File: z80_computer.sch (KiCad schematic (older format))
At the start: 14 parts, among them SW0 SW_Push, U0 Z80CPU, U1 CY62256NLL-55SNXI, U2 AT28C256_40PIN_ZIF, U4 SN74LS04N, U5 SN74LS00N, Y0 Crystal 6 MHZ

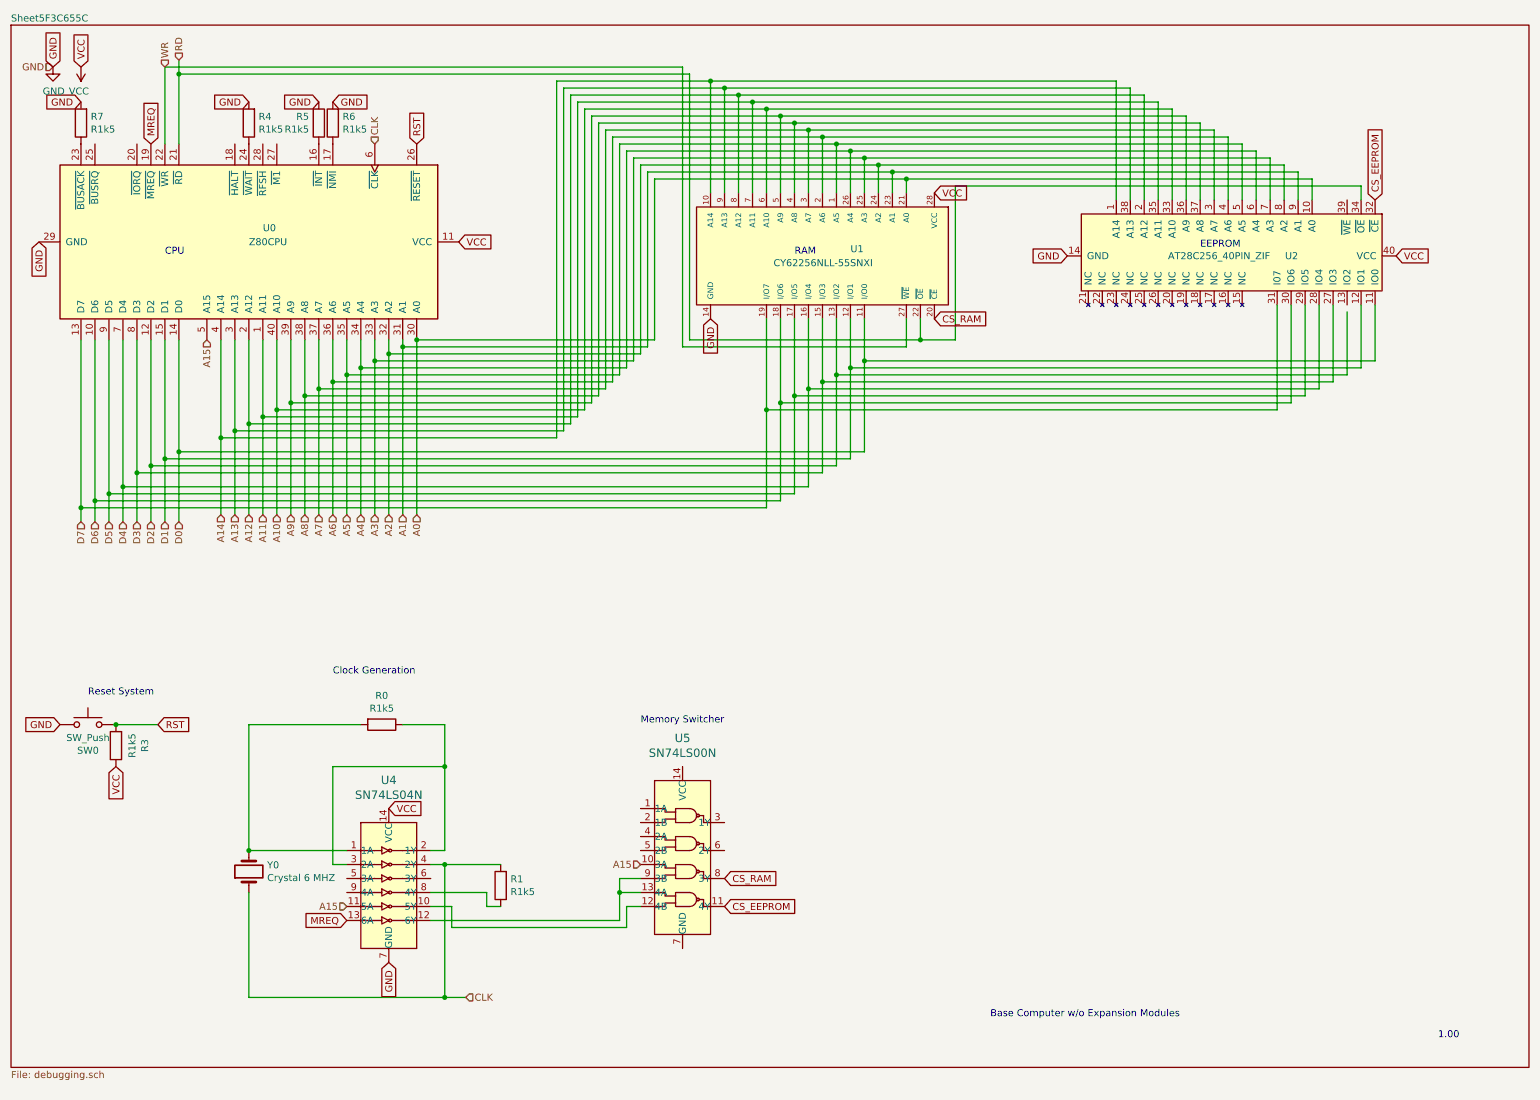
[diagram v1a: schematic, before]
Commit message: added additional schematics for submodules of the computer, So far just debugging module and the i/o expansion module
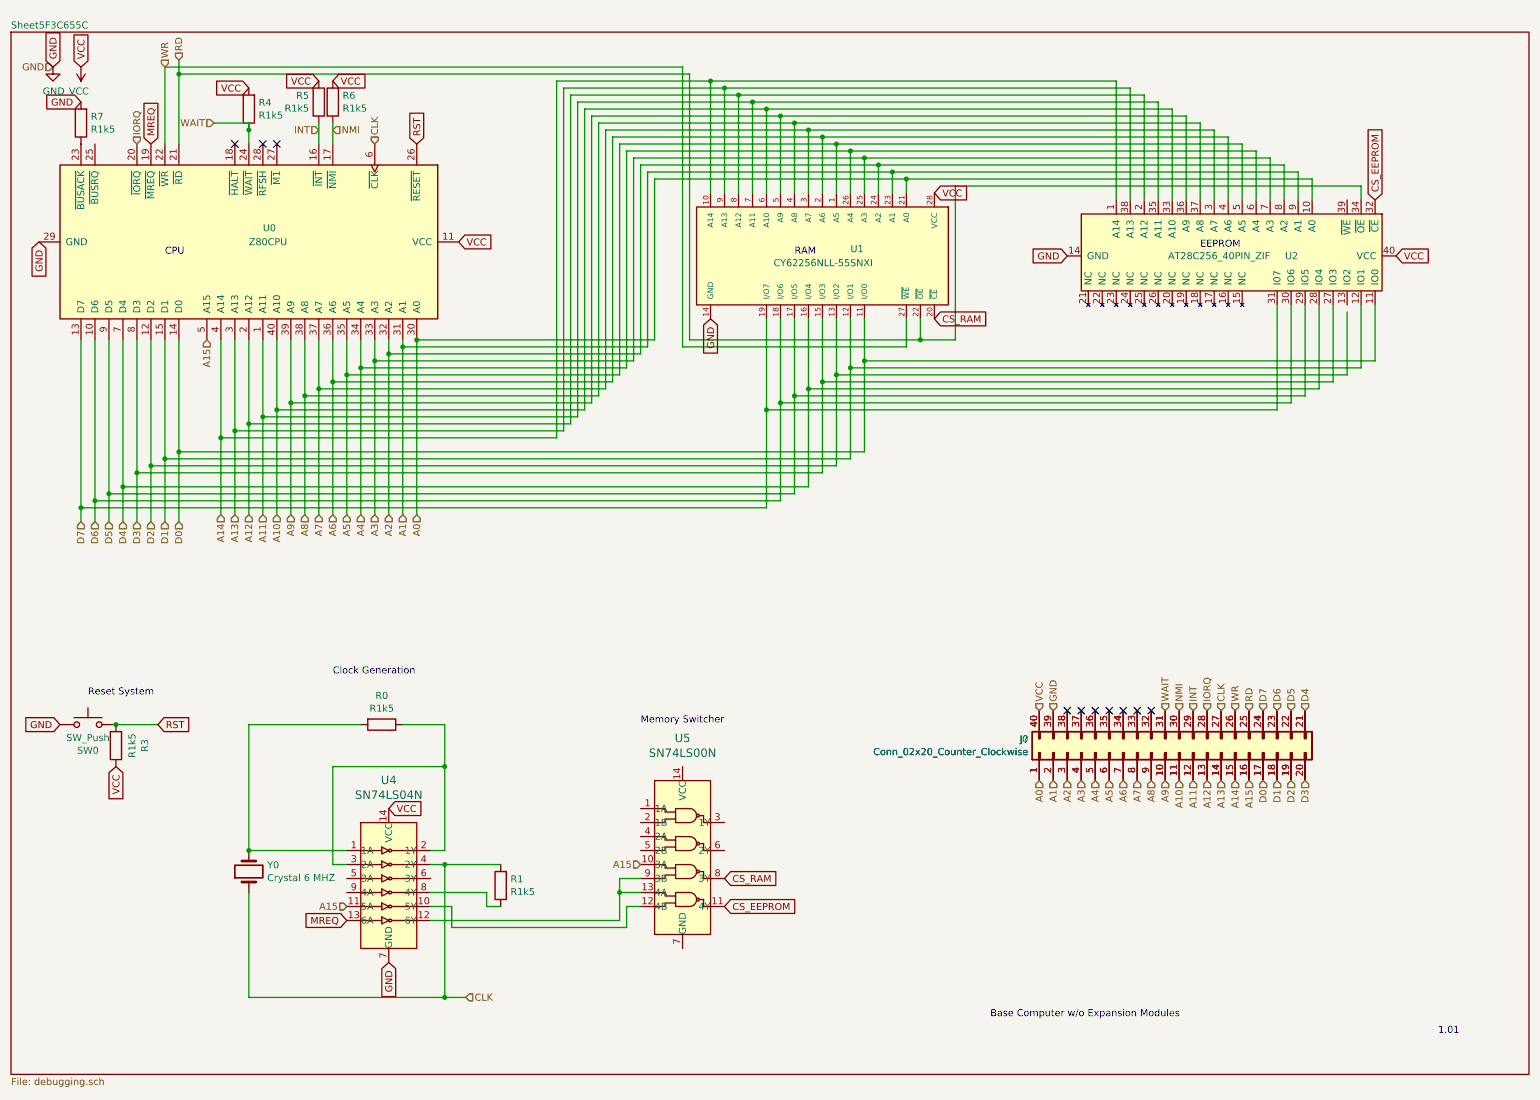
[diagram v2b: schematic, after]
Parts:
- added J0, J?: Conn_02x20_Counter_Clockwise, symbol Connector_Generic:Conn_02x20_Counter_Clockwise
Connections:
- net A0: now also J0.1 (Pin_1), J?.1 (Pin_1)
- net A1: now also J0.2 (Pin_2), J?.2 (Pin_2)
- net A10: now also J0.11 (Pin_11), J?.11 (Pin_11)
- net A11: now also J0.12 (Pin_12), J?.12 (Pin_12)
- net A12: now also J0.13 (Pin_13), J?.13 (Pin_13)
- net A13: now also J0.14 (Pin_14), J?.14 (Pin_14)
- net A14: now also J0.15 (Pin_15), J?.15 (Pin_15)
- net A15: now also J0.16 (Pin_16), J?.16 (Pin_16)
- net A2: now also J0.3 (Pin_3), J?.3 (Pin_3)
- net A3: now also J0.4 (Pin_4), J?.4 (Pin_4)
- net A4: now also J0.5 (Pin_5), J?.5 (Pin_5)
- net A5: now also J0.6 (Pin_6), J?.6 (Pin_6)
- net A6: now also J0.7 (Pin_7), J?.7 (Pin_7)
- net A7: now also J0.8 (Pin_8), J?.8 (Pin_8)
- net A8: now also J0.9 (Pin_9), J?.9 (Pin_9)
- net A9: now also J0.10 (Pin_10), J?.10 (Pin_10)
- net CLK: now also J0.27 (Pin_27), J?.27 (Pin_27)
- net D0: now also J0.17 (Pin_17), J?.17 (Pin_17)
- net D1: now also J0.18 (Pin_18), J?.18 (Pin_18)
- net D2: now also J0.19 (Pin_19), J?.19 (Pin_19)
- net D3: now also J0.20 (Pin_20), J?.20 (Pin_20)
- net D4: now also J0.21 (Pin_21), J?.21 (Pin_21)
- net D5: now also J0.22 (Pin_22), J?.22 (Pin_22)
- net D6: now also J0.23 (Pin_23), J?.23 (Pin_23)
- net D7: now also J0.24 (Pin_24), J?.24 (Pin_24)
- net GND: now also J0.39 (Pin_39), J?.39 (Pin_39); no longer R4.2, R5.2, R6.2
- net RD: now also J0.25 (Pin_25), J?.25 (Pin_25)
- net VCC: now also R4.2, R5.2, R6.2, J0.40 (Pin_40), J?.40 (Pin_40)
- net WR: now also J0.26 (Pin_26), J?.26 (Pin_26)
- net INT: now reaches R5.1, U0.16 (~INT~)
- net INT: now also J0.29 (Pin_29), J?.29 (Pin_29)
- net NMI: now reaches R6.1, U0.17 (~NMI~)
- net NMI: now also J0.30 (Pin_30), J?.30 (Pin_30)
- net IORQ: now reaches U0.20 (~IORQ~)
- net IORQ: now also J0.28 (Pin_28), J?.28 (Pin_28)
- net WAIT: now reaches R4.1, U0.24 (~WAIT~)
- net WAIT: now also J0.31 (Pin_31), J?.31 (Pin_31)
- new net: J0.32 (Pin_32), J?.32 (Pin_32)
- new net: J0.33 (Pin_33), J?.33 (Pin_33)
- new net: J0.34 (Pin_34), J?.34 (Pin_34)
- new net: J0.35 (Pin_35), J?.35 (Pin_35)
- new net: J0.36 (Pin_36), J?.36 (Pin_36)
- new net: J0.37 (Pin_37), J?.37 (Pin_37)
- new net: J0.38 (Pin_38), J?.38 (Pin_38)
- no-connect marks 0 -> 10
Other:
- note added: "1.01\n\n"
- note removed: "1.00\n"
- moved on the sheet: R4, R5, R6
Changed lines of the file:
@@
 $Descr A4 11693 8268
 encoding utf-8
-Sheet 1 2
+Sheet 1 3
 Title ""
 Date ""
@@
 L Device:R R4
 U 1 1 5F5896C9
-P 2100 1100
-F 0 "R4" H 2030 1054 50  0000 R CNN
-F 1 "R1k5" H 2030 1145 50  0000 R CNN
-F 2 "" V 2030 1100 50  0001 C CNN
-F 3 "~" H 2100 1100 50  0001 C CNN
-	1    2100 1100
+P 2100 1000
+F 0 "R4" H 2030 954 50  0000 R CNN
+F 1 "R1k5" H 2030 1045 50  0000 R CNN
+F 2 "" V 2030 1000 50  0001 C CNN
+F 3 "~" H 2100 1000 50  0001 C CNN
+	1    2100 1000
 	-1   0    0    1
 $EndComp
@@
 L Device:R R5
 U 1 1 5F598C16
-P 2600 1100
-F 0 "R5" H 2530 1054 50  0000 R CNN
-F 1 "R1k5" H 2530 1145 50  0000 R CNN
-F 2 "" V 2530 1100 50  0001 C CNN
-F 3 "~" H 2600 1100 50  0001 C CNN
-	1    2600 1100
+P 2600 950
+F 0 "R5" H 2530 904 50  0000 R CNN
+F 1 "R1k5" H 2530 995 50  0000 R CNN
+F 2 "" V 2530 950 50  0001 C CNN
+F 3 "~" H 2600 950 50  0001 C CNN
+	1    2600 950
 	1    0    0    1
 $EndComp
@@
 L Device:R R6
 U 1 1 5F5992BB
-P 2700 1100
-F 0 "R6" H 2630 1054 50  0000 R CNN
-F 1 "R1k5" H 2630 1145 50  0000 R CNN
-F 2 "" V 2630 1100 50  0001 C CNN
-F 3 "~" H 2700 1100 50  0001 C CNN
-	1    2700 1100
+P 2700 950
+F 0 "R6" H 2630 904 50  0000 R CNN
+F 1 "R1k5" H 2630 995 50  0000 R CNN
+F 2 "" V 2630 950 50  0001 C CNN
+F 3 "~" H 2700 950 50  0001 C CNN
+	1    2700 950
 	-1   0    0    1
 $EndComp
-Text GLabel 2100 950  0    50   Input ~ 0
-GND
-Text GLabel 2600 950  0    50   Input ~ 0
-GND
-Text GLabel 2700 950  2    50   Input ~ 0
-GND
+Text GLabel 2100 850  0    50   Input ~ 0
+VCC
+Text GLabel 2600 800  0    50   Input ~ 0
+VCC
+Text GLabel 2700 800  2    50   Input ~ 0
+VCC
 $Comp
 L Device:R R7
@@
 	1600 750  1600 650
 Connection ~ 1600 750
+Text Notes 10600 7700 0    50   ~ 0
+1.01\n\n
+Text HLabel 700  700  0    50   Input ~ 0
+GND
+$Comp
+L Connector_Generic:Conn_02x20_Counter_Clockwise J0
+U 1 1 5F46BF36
+P 8650 5600
+F 0 "J0" V 8746 6579 50  0000 L CNN
+F 1 "Conn_02x20_Counter_Clockwise" V 8655 6579 50  0000 L CNN
+F 2 "" H 8650 5600 50  0001 C CNN
+F 3 "~" H 8650 5600 50  0001 C CNN
+	1    8650 5600
+	0    -1   -1   0
+$EndComp
 $Sheet
-S 400  400  10850 7450
+S 400  450  10850 7450
 U 5F3C655D
 F0 "Sheet5F3C655C" 50
 F1 "debugging.sch" 50
 $EndSheet
-Text Notes 10600 7650 0    50   ~ 0
-1.00\n
-Text HLabel 700  700  0    50   Input ~ 0
+Text HLabel 7750 5800 3    50   Input ~ 0
+A0
+Text HLabel 7850 5800 3    50   Input ~ 0
+A1
+Text HLabel 7950 5800 3    50   Input ~ 0
+A2
+Text HLabel 8050 5800 3    50   Input ~ 0
+A3
+Text HLabel 8150 5800 3    50   Input ~ 0
+A4
+Text HLabel 8250 5800 3    50   Input ~ 0
+A5
+Text HLabel 8350 5800 3    50   Input ~ 0
+A6
+Text HLabel 8450 5800 3    50   Input ~ 0
+A7
+Text HLabel 8550 5800 3    50   Input ~ 0
+A8
+Text HLabel 8650 5800 3    50   Input ~ 0
+A9
+Text HLabel 8750 5800 3    50   Input ~ 0
+A10
+Text HLabel 8850 5800 3    50   Input ~ 0
+A11
+Text HLabel 8950 5800 3    50   Input ~ 0
+A12
+Text HLabel 9050 5800 3    50   Input ~ 0
+A13
+Text HLabel 9150 5800 3    50   Input ~ 0
+A14
+Text HLabel 9250 5800 3    50   Input ~ 0
+A15
+Text HLabel 9350 5800 3    50   Input ~ 0
+D0
+Text HLabel 9450 5800 3    50   Input ~ 0
+D1
+Text HLabel 9550 5800 3    50   Input ~ 0
+D2
+Text HLabel 9650 5800 3    50   Input ~ 0
+D3
+Text HLabel 9650 5300 1    50   Input ~ 0
+D4
+Text HLabel 9550 5300 1    50   Input ~ 0
+D5
+Text HLabel 9450 5300 1    50   Input ~ 0
+D6
+Text HLabel 9350 5300 1    50   Input ~ 0
+D7
+Text HLabel 9250 5300 1    50   Input ~ 0
+RD
+Text HLabel 9150 5300 1    50   Input ~ 0
+WR
+Text HLabel 9050 5300 1    50   Input ~ 0
+CLK
+Text HLabel 8950 5300 1    50   Input ~ 0
+IORQ
+Text HLabel 1300 1250 1    50   Input ~ 0
+IORQ
+Text HLabel 1850 1100 0    50   Input ~ 0
+WAIT
+Wire Wire Line
+	1850 1100 2100 1100
+Wire Wire Line
+	2100 1100 2100 1150
+Wire Wire Line
+	2100 1250 2100 1150
+Connection ~ 2100 1150
+Wire Wire Line
+	2600 1250 2600 1100
+Text HLabel 2600 1150 0    50   Input ~ 0
+INT
+Wire Wire Line
+	2700 1100 2700 1250
+Text HLabel 2700 1150 2    50   Input ~ 0
+NMI
+Text HLabel 8850 5300 1    50   Input ~ 0
+INT
+Text HLabel 8750 5300 1    50   Input ~ 0
+NMI
+Text HLabel 8650 5300 1    50   Input ~ 0
+WAIT
+Text HLabel 7750 5300 1    50   Input ~ 0
+VCC
+Text HLabel 7850 5300 1    50   Input ~ 0
 GND
+NoConn ~ 7950 5300
+NoConn ~ 8050 5300
+NoConn ~ 8150 5300
+NoConn ~ 8250 5300
+NoConn ~ 8350 5300
+NoConn ~ 8450 5300
+NoConn ~ 8550 5300
+NoConn ~ 2000 1250
+NoConn ~ 2200 1250
+NoConn ~ 2300 1250
+$Comp
+L Connector_Generic:Conn_02x20_Counter_Clockwise J?
+U 1 1 5F63C129
+P 8650 5600
+F 0 "J?" V 8746 6579 50  0000 L CNN
+F 1 "Conn_02x20_Counter_Clockwise" V 8655 6579 50  0000 L CNN
+F 2 "" H 8650 5600 50  0001 C CNN
+F 3 "~" H 8650 5600 50  0001 C CNN
+	1    8650 5600
+	0    -1   -1   0
+$EndComp
 $EndSCHEMATC
